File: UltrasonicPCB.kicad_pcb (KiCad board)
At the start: 2 copper layers, 65 x 56 mm, 13 parts, among them J1 Conn_01x10

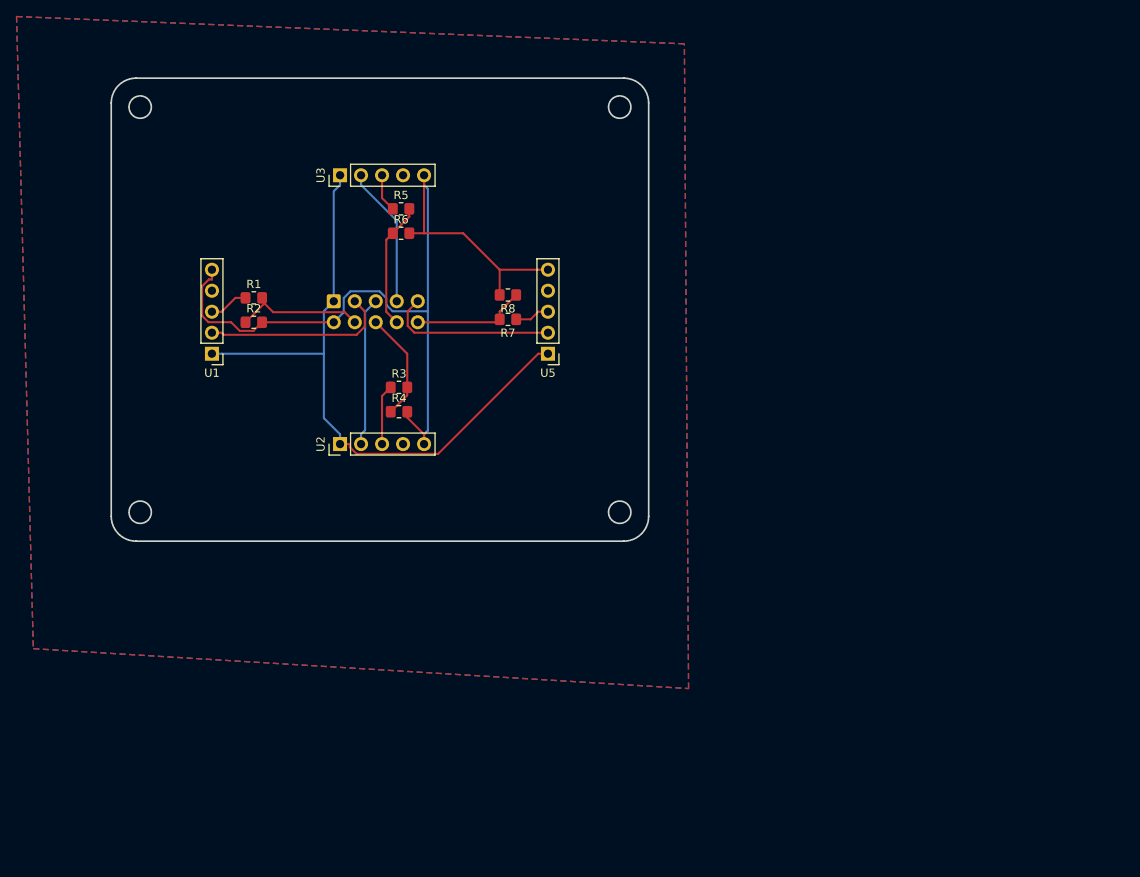
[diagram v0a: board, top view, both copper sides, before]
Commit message: Updated with 1 echo
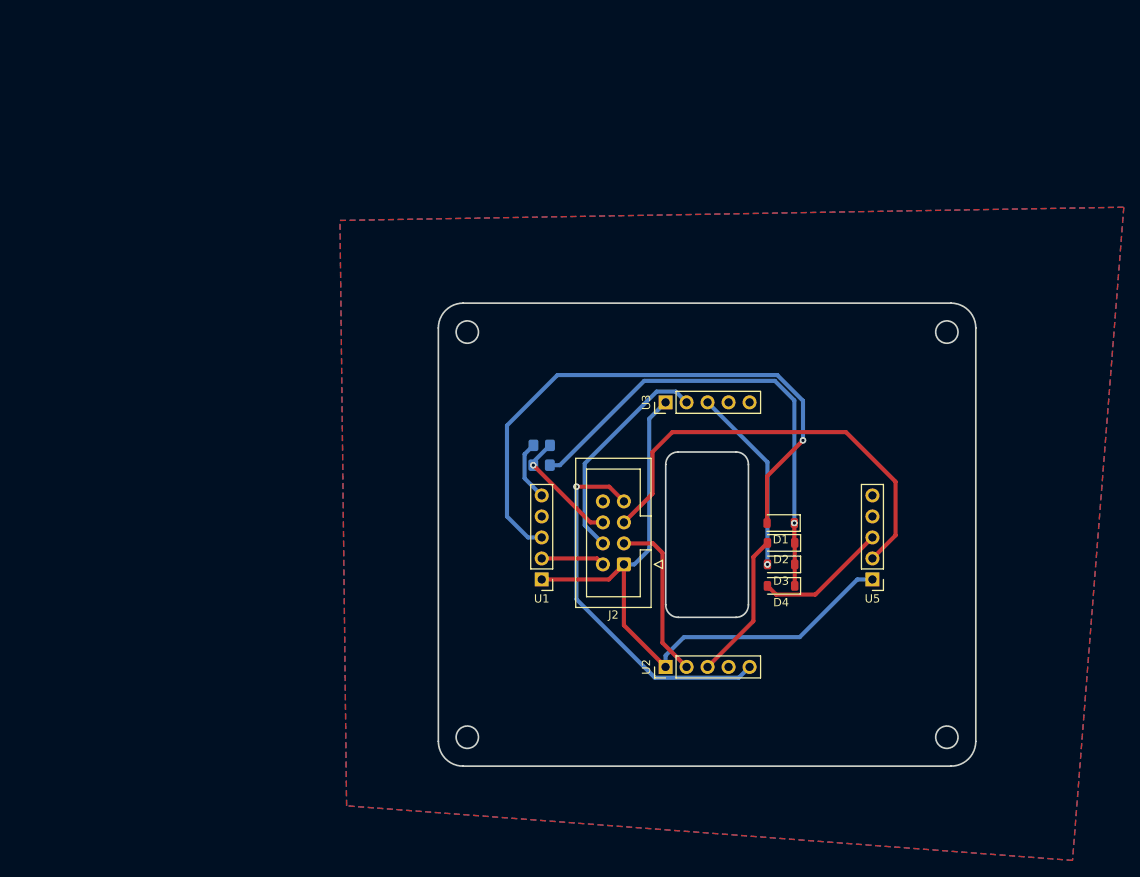
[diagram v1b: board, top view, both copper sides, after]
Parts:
- removed J1: Conn_01x10, Connector_IDC:IDC-Header_2x05_P2.54mm_Vertical
- removed R3, R4, R5, R6, R7, R8: R, Resistor_SMD:R_0805_2012Metric_Pad1.20x1.40mm_HandSolder
- added D1: 1N4148WT, Diode_SMD:D_SOD-123, F.Cu at (138.9, 98.6)
- added D2: 1N4148WT, Diode_SMD:D_SOD-123, F.Cu at (138.9, 101.0)
- added D3: 1N4148WT, Diode_SMD:D_SOD-123, F.Cu at (138.9, 103.6)
- added D4: 1N4148WT, Diode_SMD:D_SOD-123, F.Cu at (138.9, 106.2)
- added J2: Conn_01x07, Connector_IDC:IDC-Header_2x04_P2.54mm_Vertical, F.Cu at (119.9, 103.6)
- R1, R2: moved to B.Cu
- moved U1 48.3 mm to (110.0, 105.4)
- moved U3 48.0 mm to (125.0, 84.0)
- moved U5 47.8 mm to (150.0, 105.4)
- moved U2 47.7 mm to (125.0, 116.0)
- moved R1 40.3 mm to (110.0, 91.6), turned to 180 degrees
- moved R2 37.9 mm to (110.0, 89.2), turned to 180 degrees
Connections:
- net ECHO1 renamed Net-(J2-Pin_6)
- R1 pad 1: Net-(U1-ECHO) -> ECHO
- U1 pad 3: Net-(U1-ECHO) -> Net-(D1-A)
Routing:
- net Net-(D1-A): track 0.00 -> 72.5 mm, vias 0 -> 1
- net ECHO: track 0.00 -> 57.2 mm, vias 0 -> 1
- net GND: track 105.1 -> 52.9 mm, vias 0 -> 1
- net TRIG4: track 20.8 -> 53.3 mm
- net Net-(D3-A): track 4.60 -> 22.6 mm, vias 0 -> 1
- net ECHO3: track 15.4 -> 0.00 mm
- net TRIG1: track 22.6 -> 7.70 mm
- net ECHO4: track 13.8 -> 0.00 mm
- net ECHO2: track 13.2 -> 0.00 mm
- net Net-(D4-A): track 4.22 -> 16.0 mm
- net Net-(D2-A): track 7.29 -> 18.0 mm
- net TRIG3: track 17.0 -> 27.0 mm
- net Net-(U1-ECHO): track 4.76 -> 0.00 mm
- net TRIG2: track 18.0 -> 20.1 mm
- net Net-(J2-Pin_6): track 15.9 -> 14.5 mm, vias 0 -> 1
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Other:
- outline, holes or cut-outs redrawn

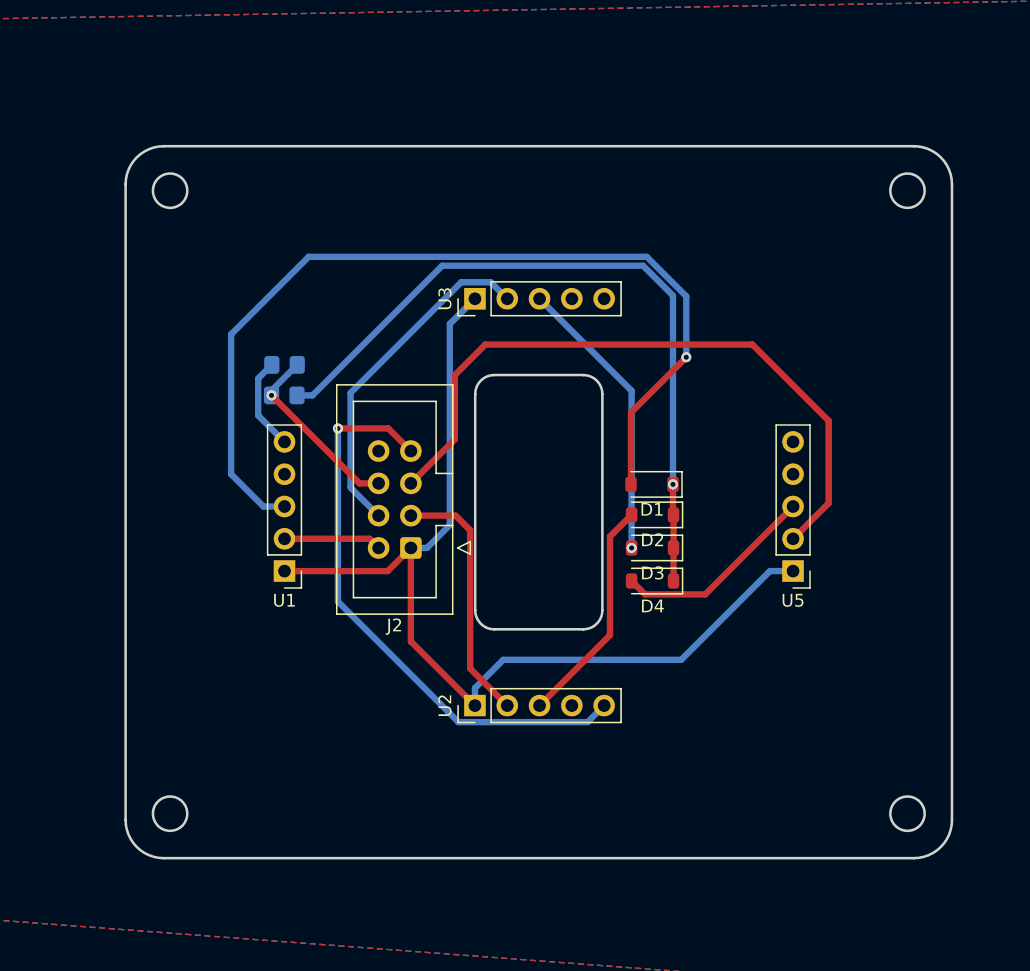
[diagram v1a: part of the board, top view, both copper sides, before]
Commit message: Changed Outline
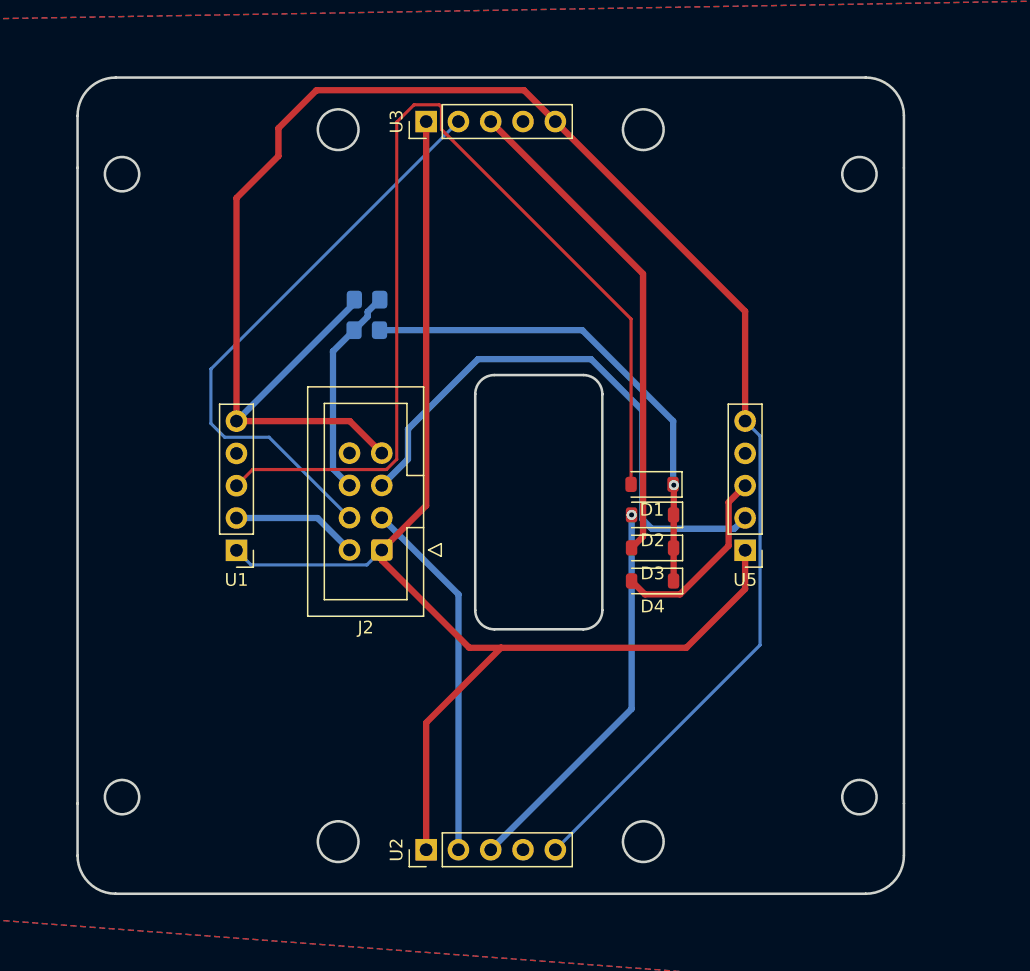
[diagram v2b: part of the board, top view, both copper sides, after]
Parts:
- moved U3 14.5 mm to (121.1, 70.1)
- moved U2 12.0 mm to (121.1, 127.3)
- moved R2 8.27 mm to (116.5, 84.1)
- moved R1 8.27 mm to (116.5, 86.5)
- moved U1 4.12 mm to (106.2, 103.8)
- moved U5 4.11 mm to (146.2, 103.8)
- moved J2 2.30 mm to (117.7, 103.8)
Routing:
- net GND: track 52.9 -> 144.9 mm, vias 1 -> 0
- net 5V: track 77.8 -> 103.1 mm
- net TRIG3: track 27.0 -> 45.8 mm
- net ECHO: track 57.2 -> 38.7 mm
- net Net-(D3-A): track 22.6 -> 38.9 mm, vias 1 -> 0
- net Net-(D2-A): track 18.0 -> 31.0 mm, vias 0 -> 1
- net TRIG2: track 20.1 -> 28.6 mm
- net TRIG4: track 53.3 -> 45.0 mm
- net Net-(D1-A): track 72.5 -> 80.0 mm, vias 1 -> 0
- net TRIG1: track 7.70 -> 9.93 mm
- net Net-(J2-Pin_6): track 14.5 -> 16.7 mm, vias 1 -> 0
- net Net-(D4-A): track 16.0 -> 14.9 mm
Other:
- board size 65 x 56 mm -> 65 x 64.2 mm

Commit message: 2nd Revision
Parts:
- J2: moved to B.Cu
- moved D4 14.7 mm to (151.9, 99.3), turned to -90 degrees
- moved J2 2.06 mm to (115.6, 103.7), turned to 0 degrees
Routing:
- net ECHO: track 38.7 -> 161.9 mm
- net 5V: track 103.1 -> 148.3 mm
- net GND: track 144.9 -> 167.8 mm
- net Net-(D1-A): track 80.0 -> 59.9 mm
- net Net-(D2-A): track 31.0 -> 44.6 mm, vias 1 -> 0
- net TRIG3: track 45.8 -> 35.8 mm
- net Net-(D4-A): track 14.9 -> 19.6 mm
- net TRIG4: track 45.0 -> 49.6 mm
- net TRIG1: track 9.93 -> 14.1 mm
- net TRIG2: track 28.6 -> 30.6 mm
- net Net-(J2-Pin_6): track 16.7 -> 17.6 mm, vias 0 -> 1
